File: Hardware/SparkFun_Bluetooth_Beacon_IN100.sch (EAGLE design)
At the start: 33 parts, among them J3 Vertical Qwiic Connector, U1 IN100, Y1 CRYSTAL-26MHZSMD-3.2X2.5

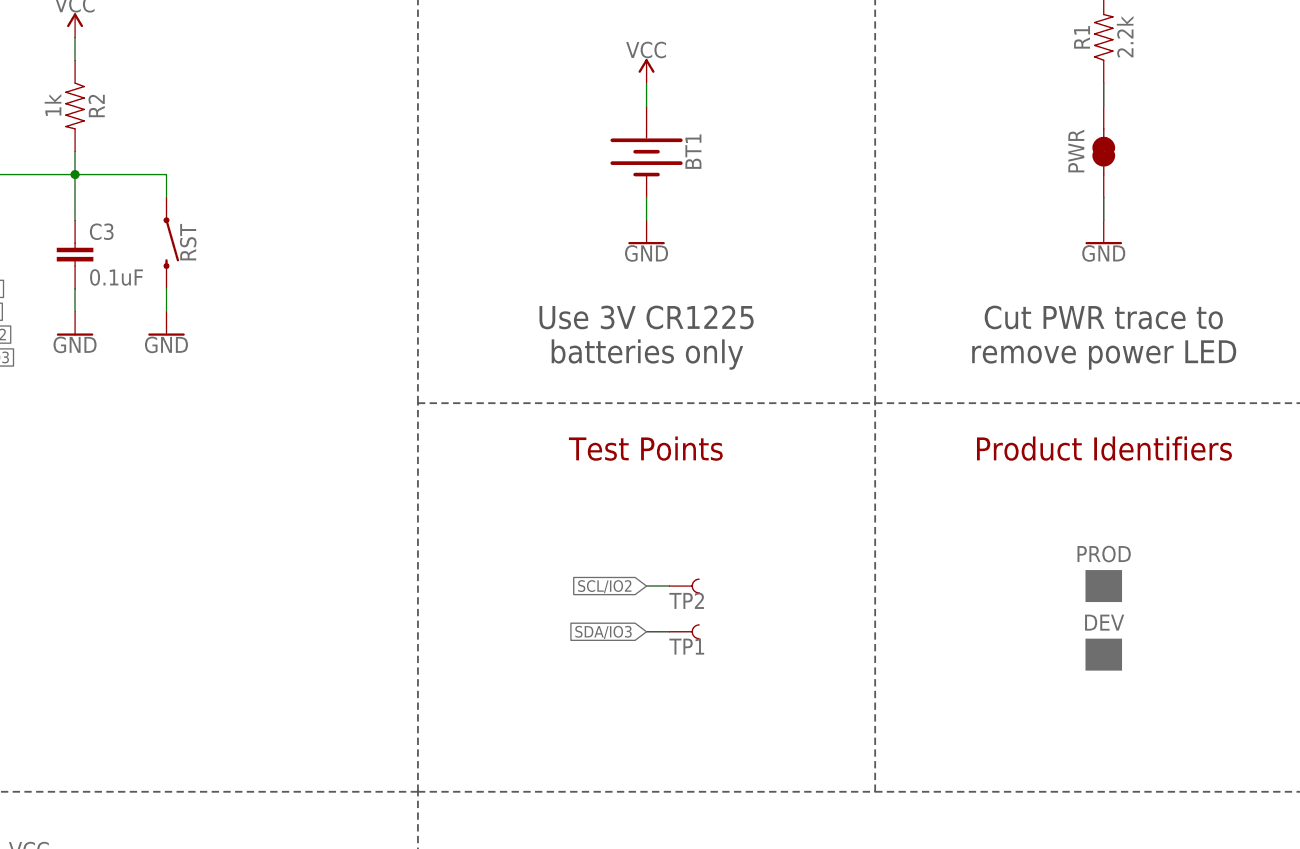
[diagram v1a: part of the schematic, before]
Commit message: Add EN test point
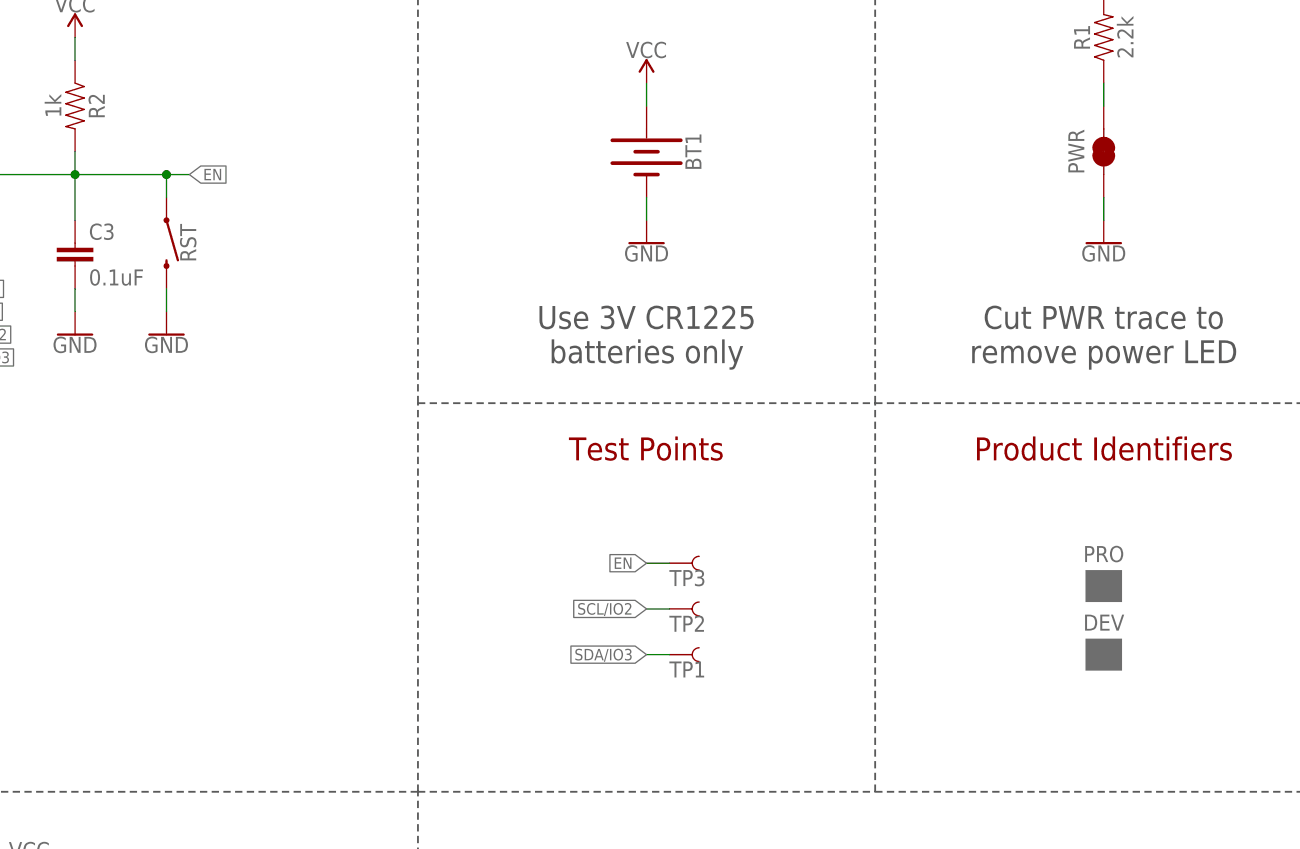
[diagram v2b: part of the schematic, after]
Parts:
- added TP3: TEST-POINT3, SparkFun-Connectors:TEST-POINT3
- renumbered PROD to PRO
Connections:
- net EN: now also TP3.1
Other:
- moved on the sheet: TP1, TP2
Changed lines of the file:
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@@
 <part name="GND12" library="SparkFun-PowerSymbols" deviceset="GND" device=""/>
 <part name="LOGO3" library="SparkFun-Aesthetics" deviceset="QWIIC_LOGO" device="_3MM"/>
-<part name="PROD" library="SparkFun-Aesthetics" deviceset="PROD_ID_PASTE" device="_SILK" value="PROD_ID_PASTE_SILK"/>
+<part name="PRO" library="SparkFun-Aesthetics" deviceset="PROD_ID_PASTE" device="_SILK" value="PROD_ID_PASTE_SILK"/>
 <part name="DEV" library="SparkFun-Aesthetics" deviceset="PROD_ID_PASTE" device="_SILK"/>
+<part name="TP3" library="SparkFun-Connectors" deviceset="TEST-POINT" device="3"/>
 </parts>
 <sheets>
@@
 <attribute name="VALUE" x="105.664" y="33.02" size="1.778" layer="96" font="vector" rot="R90" align="top-center"/>
 </instance>
-<instance part="TP1" gate="G$1" x="175.26" y="86.36" smashed="yes">
-<attribute name="NAME" x="175.26" y="83.82" size="1.778" layer="95" font="vector"/>
-</instance>
-<instance part="TP2" gate="G$1" x="175.26" y="91.44" smashed="yes">
-<attribute name="NAME" x="175.26" y="88.9" size="1.778" layer="95" font="vector"/>
+<instance part="TP1" gate="G$1" x="175.26" y="83.82" smashed="yes">
+<attribute name="NAME" x="175.26" y="81.28" size="1.778" layer="95" font="vector"/>
+</instance>
+<instance part="TP2" gate="G$1" x="175.26" y="88.9" smashed="yes">
+<attribute name="NAME" x="175.26" y="86.36" size="1.778" layer="95" font="vector"/>
 </instance>
 <instance part="BUS" gate="G$1" x="96.52" y="55.88" smashed="yes" rot="MR90">
@@
 </instance>
 <instance part="LOGO3" gate="G$1" x="180.34" y="43.18" smashed="yes"/>
-<instance part="PROD" gate="G$1" x="223.52" y="91.44" smashed="yes">
+<instance part="PRO" gate="G$1" x="223.52" y="91.44" smashed="yes">
 <attribute name="NAME" x="223.52" y="94.996" size="1.778" layer="95" font="vector" align="center"/>
 </instance>
 <instance part="DEV" gate="G$1" x="223.52" y="83.82" smashed="yes">
 <attribute name="NAME" x="223.52" y="87.376" size="1.778" layer="95" font="vector" align="center"/>
+</instance>
+<instance part="TP3" gate="G$1" x="175.26" y="93.98" smashed="yes">
+<attribute name="NAME" x="175.26" y="91.44" size="1.778" layer="95" font="vector"/>
 </instance>
 </instances>
@@
 <segment>
 <pinref part="TP2" gate="G$1" pin="1"/>
-<wire x1="175.26" y1="91.44" x2="172.72" y2="91.44" width="0.1524" layer="91"/>
-<label x="172.72" y="91.44" size="1.27" layer="95" font="vector" rot="R180" xref="yes"/>
+<wire x1="175.26" y1="88.9" x2="172.72" y2="88.9" width="0.1524" layer="91"/>
+<label x="172.72" y="88.9" size="1.27" layer="95" font="vector" rot="R180" xref="yes"/>
 </segment>
 </net>
@@
 <segment>
 <pinref part="TP1" gate="G$1" pin="1"/>
-<wire x1="175.26" y1="86.36" x2="172.72" y2="86.36" width="0.1524" layer="91"/>
-<label x="172.72" y="86.36" size="1.27" layer="95" font="vector" rot="R180" xref="yes"/>
+<wire x1="175.26" y1="83.82" x2="172.72" y2="83.82" width="0.1524" layer="91"/>
+<label x="172.72" y="83.82" size="1.27" layer="95" font="vector" rot="R180" xref="yes"/>
 </segment>
 </net>
@@
 <wire x1="119.38" y1="134.62" x2="119.38" y2="137.16" width="0.1524" layer="91"/>
 <wire x1="109.22" y1="137.16" x2="119.38" y2="137.16" width="0.1524" layer="91"/>
-</segment>
-</net>
+<wire x1="119.38" y1="137.16" x2="121.92" y2="137.16" width="0.1524" layer="91"/>
+<junction x="119.38" y="137.16"/>
+<label x="121.92" y="137.16" size="1.27" layer="95" font="vector" xref="yes"/>
+</segment>
+<segment>
+<pinref part="TP3" gate="G$1" pin="1"/>
+<wire x1="175.26" y1="93.98" x2="172.72" y2="93.98" width="0.1524" layer="91"/>
+<label x="172.72" y="93.98" size="1.27" layer="95" font="vector" rot="R180" xref="yes"/>
+</segment>
+</net>
